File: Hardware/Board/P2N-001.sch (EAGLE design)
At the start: 37 parts, among them IC1 4053N, IC2 LTC485N, IC3 74LS07N, IC4 LTC485N, K1 G5V1, T1 2SC1815

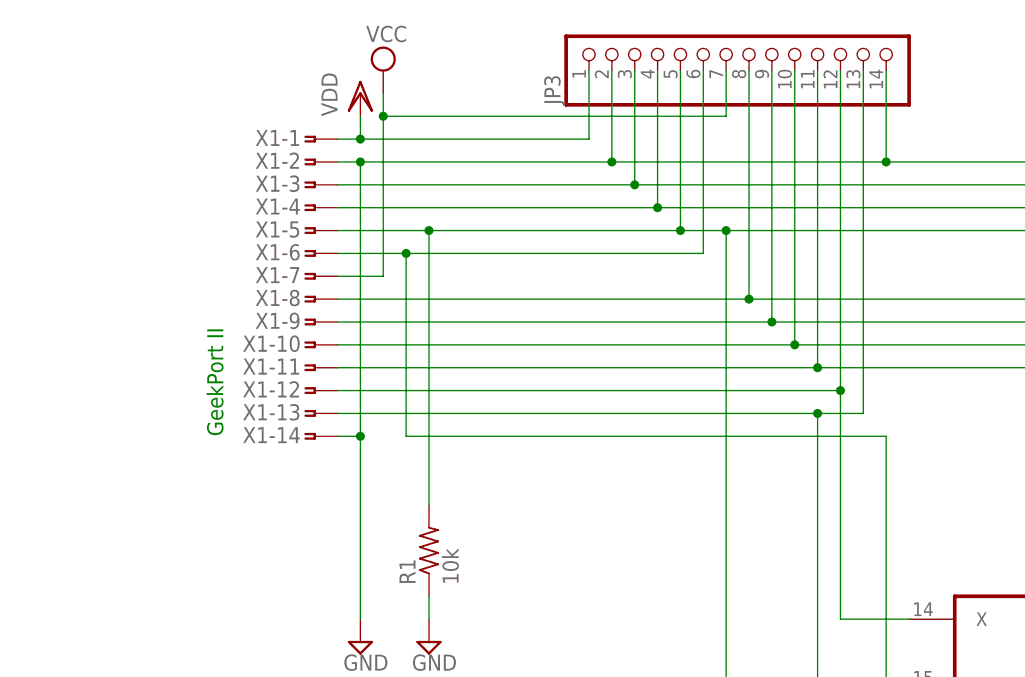
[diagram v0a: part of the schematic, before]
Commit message: Updated Hirose DX10LM1-14SE connector pattern.
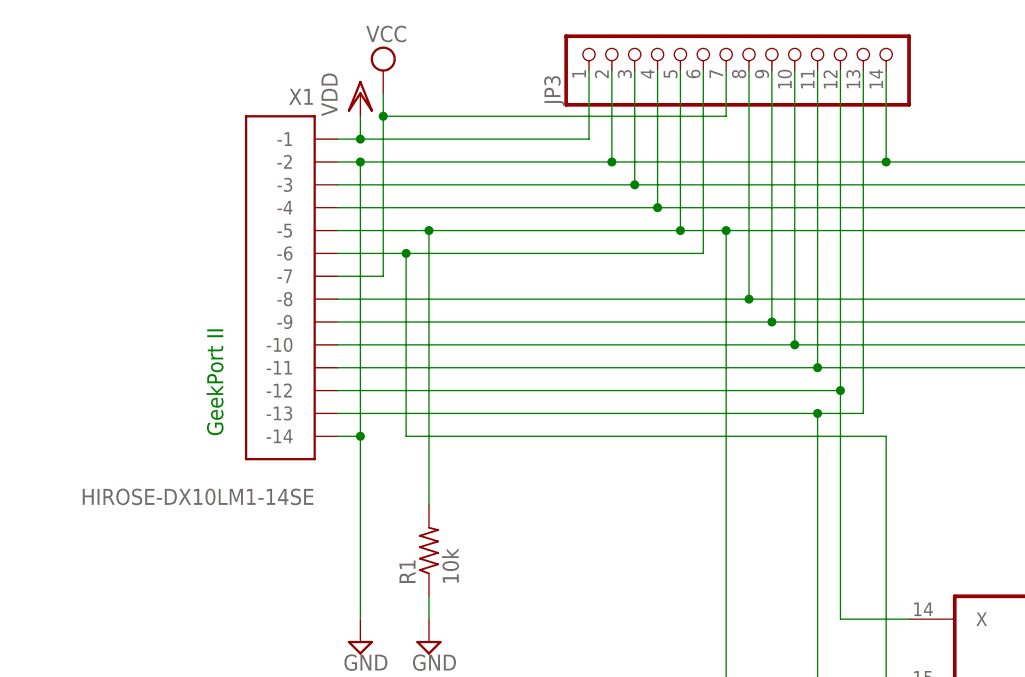
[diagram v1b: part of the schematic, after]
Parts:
- X1: value (none) -> HIROSE-DX10LM1-14SE; device con-hirose-dxlm:HIROSE-DXLM -> con-hirose-dx10lm1-14se:HIROSE-DX10LM1-14SE
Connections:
- net ANLG0: now also X1.-8; no longer X1-8.1
- net ANLG1: now also X1.-9; no longer X1-9.1
- net ANLG2: now also X1.-10; no longer X1-10.1
- net ANLG3: now also X1.-11; no longer X1-11.1
- net CD: now also X1.-6; no longer X1-6.1
- net GND: now also X1.-14, X1.-2; no longer X1-14.1, X1-2.1
- net N$28: now also X1.-12; no longer X1-12.1
- net N$29: now also X1.-13; no longer X1-13.1
- net PD: now also X1.-5; no longer X1-5.1
- net USBD+: now also X1.-3; no longer X1-3.1
- net USBD-: now also X1.-4; no longer X1-4.1
- net VCC: now also X1.-7; no longer X1-7.1
- net VDD: now also X1.-1; no longer X1-1.1
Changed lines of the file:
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@@
 <part name="SUPPLY2" library="supply2" deviceset="GND" device=""/>
 <part name="SUPPLY29" library="supply2" deviceset="GND" device=""/>
-<part name="X1" library="con-hirose-dxlm" deviceset="HIROSE-DXLM" device=""/>
 <part name="VDD1" library="supply1" deviceset="VDD" device=""/>
 <part name="SUPPLY5" library="supply2" deviceset="GND" device=""/>
@@
 <part name="SUPPLY8" library="supply2" deviceset="GND" device=""/>
 <part name="R9" library="resistor" deviceset="R-US_" device="0204/5" value="220"/>
+<part name="X1" library="con-hirose-dx10lm1-14se" deviceset="HIROSE-DX10LM1-14SE" device=""/>
 </parts>
 <sheets>
@@
 <instance part="SUPPLY2" gate="GND" x="25.4" y="129.54"/>
 <instance part="SUPPLY29" gate="GND" x="297.18" y="101.6"/>
-<instance part="X1" gate="-1" x="20.32" y="185.42" rot="MR0"/>
-<instance part="X1" gate="-2" x="20.32" y="182.88" rot="MR0"/>
-<instance part="X1" gate="-3" x="20.32" y="180.34" rot="MR0"/>
-<instance part="X1" gate="-4" x="20.32" y="177.8" rot="MR0"/>
-<instance part="X1" gate="-5" x="20.32" y="175.26" rot="MR0"/>
-<instance part="X1" gate="-6" x="20.32" y="172.72" rot="MR0"/>
-<instance part="X1" gate="-7" x="20.32" y="170.18" rot="MR0"/>
-<instance part="X1" gate="-8" x="20.32" y="167.64" rot="MR0"/>
-<instance part="X1" gate="-9" x="20.32" y="165.1" rot="MR0"/>
-<instance part="X1" gate="-10" x="20.32" y="162.56" rot="MR0"/>
-<instance part="X1" gate="-11" x="20.32" y="160.02" rot="MR0"/>
-<instance part="X1" gate="-12" x="20.32" y="157.48" rot="MR0"/>
-<instance part="X1" gate="-13" x="20.32" y="154.94" rot="MR0"/>
-<instance part="X1" gate="-14" x="20.32" y="152.4" rot="MR0"/>
 <instance part="VDD1" gate="G$1" x="7.62" y="114.3"/>
 <instance part="SUPPLY5" gate="GND" x="40.64" y="93.98"/>
@@
 <instance part="SUPPLY8" gate="GND" x="91.44" y="7.62"/>
 <instance part="R9" gate="G$1" x="228.6" y="104.14"/>
+<instance part="X1" gate="G$1" x="17.78" y="154.94" rot="MR0"/>
 </instances>
 <busses>
@@
 </segment>
 <segment>
-<pinref part="X1" gate="-2" pin="1"/>
 <pinref part="SUPPLY2" gate="GND" pin="GND"/>
 <wire x1="22.86" y1="182.88" x2="25.4" y2="182.88" width="0.1524" layer="91"/>
 <wire x1="25.4" y1="182.88" x2="25.4" y2="152.4" width="0.1524" layer="91"/>
-<pinref part="X1" gate="-14" pin="1"/>
 <wire x1="25.4" y1="152.4" x2="25.4" y2="132.08" width="0.1524" layer="91"/>
 <wire x1="22.86" y1="152.4" x2="25.4" y2="152.4" width="0.1524" layer="91"/>
@@
 <wire x1="83.82" y1="193.04" x2="83.82" y2="182.88" width="0.1524" layer="91"/>
 <junction x="83.82" y="182.88"/>
+<pinref part="X1" gate="G$1" pin="-2"/>
+<pinref part="X1" gate="G$1" pin="-14"/>
 </segment>
 <segment>
@@
 <pinref part="SUPPLY3" gate="G$1" pin="VCC"/>
 <wire x1="27.94" y1="190.5" x2="27.94" y2="187.96" width="0.1524" layer="91"/>
-<pinref part="X1" gate="-7" pin="1"/>
 <wire x1="27.94" y1="187.96" x2="27.94" y2="170.18" width="0.1524" layer="91"/>
 <wire x1="27.94" y1="170.18" x2="22.86" y2="170.18" width="0.1524" layer="91"/>
@@
 <wire x1="66.04" y1="187.96" x2="66.04" y2="193.04" width="0.1524" layer="91"/>
 <junction x="27.94" y="187.96"/>
+<pinref part="X1" gate="G$1" pin="-7"/>
 </segment>
 <segment>
@@
 </segment>
 <segment>
-<pinref part="X1" gate="-1" pin="1"/>
 <pinref part="VDD3" gate="G$1" pin="VDD"/>
 <wire x1="22.86" y1="185.42" x2="25.4" y2="185.42" width="0.1524" layer="91"/>
@@
 <wire x1="50.8" y1="185.42" x2="50.8" y2="193.04" width="0.1524" layer="91"/>
 <junction x="25.4" y="185.42"/>
+<pinref part="X1" gate="G$1" pin="-1"/>
 </segment>
 <segment>
@@
 </segment>
 <segment>
-<pinref part="X1" gate="-8" pin="1"/>
 <wire x1="127" y1="165.1" x2="124.46" y2="167.64" width="0.1524" layer="91" curve="90"/>
 <wire x1="124.46" y1="167.64" x2="68.58" y2="167.64" width="0.1524" layer="91"/>
@@
 <wire x1="68.58" y1="193.04" x2="68.58" y2="167.64" width="0.1524" layer="91"/>
 <junction x="68.58" y="167.64"/>
+<pinref part="X1" gate="G$1" pin="-8"/>
 </segment>
 </net>
@@
 </segment>
 <segment>
-<pinref part="X1" gate="-9" pin="1"/>
 <wire x1="127" y1="162.56" x2="124.46" y2="165.1" width="0.1524" layer="91" curve="90"/>
 <wire x1="124.46" y1="165.1" x2="71.12" y2="165.1" width="0.1524" layer="91"/>
@@
 <wire x1="71.12" y1="193.04" x2="71.12" y2="165.1" width="0.1524" layer="91"/>
 <junction x="71.12" y="165.1"/>
+<pinref part="X1" gate="G$1" pin="-9"/>
 </segment>
 </net>
@@
 </segment>
 <segment>
-<pinref part="X1" gate="-10" pin="1"/>
 <wire x1="127" y1="160.02" x2="124.46" y2="162.56" width="0.1524" layer="91" curve="90"/>
 <wire x1="124.46" y1="162.56" x2="73.66" y2="162.56" width="0.1524" layer="91"/>
@@
 <wire x1="73.66" y1="193.04" x2="73.66" y2="162.56" width="0.1524" layer="91"/>
 <junction x="73.66" y="162.56"/>
+<pinref part="X1" gate="G$1" pin="-10"/>
 </segment>
 </net>
@@
 </segment>
 <segment>
-<pinref part="X1" gate="-11" pin="1"/>
 <wire x1="127" y1="157.48" x2="124.46" y2="160.02" width="0.1524" layer="91" curve="90"/>
 <wire x1="124.46" y1="160.02" x2="76.2" y2="160.02" width="0.1524" layer="91"/>
@@
 <wire x1="76.2" y1="193.04" x2="76.2" y2="160.02" width="0.1524" layer="91"/>
 <junction x="76.2" y="160.02"/>
+<pinref part="X1" gate="G$1" pin="-11"/>
 </segment>
 </net>
@@
 <net name="PD" class="0">
 <segment>
-<pinref part="X1" gate="-5" pin="1"/>
 <pinref part="JP6" gate="A" pin="1"/>
 <wire x1="22.86" y1="175.26" x2="33.02" y2="175.26" width="0.1524" layer="91"/>
@@
 <label x="81.28" y="83.82" size="1.778" layer="95" rot="R90"/>
 <junction x="66.04" y="175.26"/>
+<pinref part="X1" gate="G$1" pin="-5"/>
 </segment>
 </net>
 <net name="USBD-" class="0">
 <segment>
-<pinref part="X1" gate="-4" pin="1"/>
 <pinref part="JP6" gate="A" pin="2"/>
 <wire x1="22.86" y1="177.8" x2="58.42" y2="177.8" width="0.1524" layer="91"/>
@@
 <junction x="58.42" y="177.8"/>
 <label x="111.76" y="177.8" size="1.778" layer="95"/>
+<pinref part="X1" gate="G$1" pin="-4"/>
 </segment>
 </net>
 <net name="USBD+" class="0">
 <segment>
-<pinref part="X1" gate="-3" pin="1"/>
 <pinref part="JP6" gate="A" pin="3"/>
 <wire x1="22.86" y1="180.34" x2="55.88" y2="180.34" width="0.1524" layer="91"/>
@@
 <junction x="55.88" y="180.34"/>
 <label x="111.76" y="180.34" size="1.778" layer="95"/>
+<pinref part="X1" gate="G$1" pin="-3"/>
 </segment>
 </net>
 <net name="CD" class="0">
 <segment>
-<pinref part="X1" gate="-6" pin="1"/>
 <wire x1="22.86" y1="172.72" x2="30.48" y2="172.72" width="0.1524" layer="91"/>
 <wire x1="30.48" y1="172.72" x2="30.48" y2="152.4" width="0.1524" layer="91"/>
@@
 <label x="78.74" y="55.88" size="1.778" layer="95"/>
 <label x="83.82" y="83.82" size="1.778" layer="95" rot="R90"/>
+<pinref part="X1" gate="G$1" pin="-6"/>
 </segment>
 </net>
 <net name="N$28" class="0">
 <segment>
-<pinref part="X1" gate="-12" pin="1"/>
 <wire x1="22.86" y1="157.48" x2="78.74" y2="157.48" width="0.1524" layer="91"/>
 <wire x1="78.74" y1="157.48" x2="78.74" y2="132.08" width="0.1524" layer="91"/>
@@
 <wire x1="78.74" y1="193.04" x2="78.74" y2="157.48" width="0.1524" layer="91"/>
 <junction x="78.74" y="157.48"/>
+<pinref part="X1" gate="G$1" pin="-12"/>
 </segment>
 </net>
 <net name="N$29" class="0">
 <segment>
-<pinref part="X1" gate="-13" pin="1"/>
 <wire x1="22.86" y1="154.94" x2="76.2" y2="154.94" width="0.1524" layer="91"/>
 <wire x1="76.2" y1="154.94" x2="76.2" y2="124.46" width="0.1524" layer="91"/>
@@
 <wire x1="76.2" y1="124.46" x2="86.36" y2="124.46" width="0.1524" layer="91"/>
 <wire x1="76.2" y1="154.94" x2="81.28" y2="154.94" width="0.1524" layer="91"/>
-<wire x1="81.28" y1="154.94" x2="81.28" y2="175.26" width="0.1524" layer="91"/>
+<wire x1="81.28" y1="154.94" x2="81.28" y2="193.04" width="0.1524" layer="91"/>
 <pinref part="JP3" gate="A" pin="13"/>
 <junction x="76.2" y="154.94"/>
-<wire x1="81.28" y1="175.26" x2="81.28" y2="193.04" width="0.1524" layer="91"/>
-</segment>
-</net>
+<pinref part="X1" gate="G$1" pin="-13"/>
+</segment>
+</net>

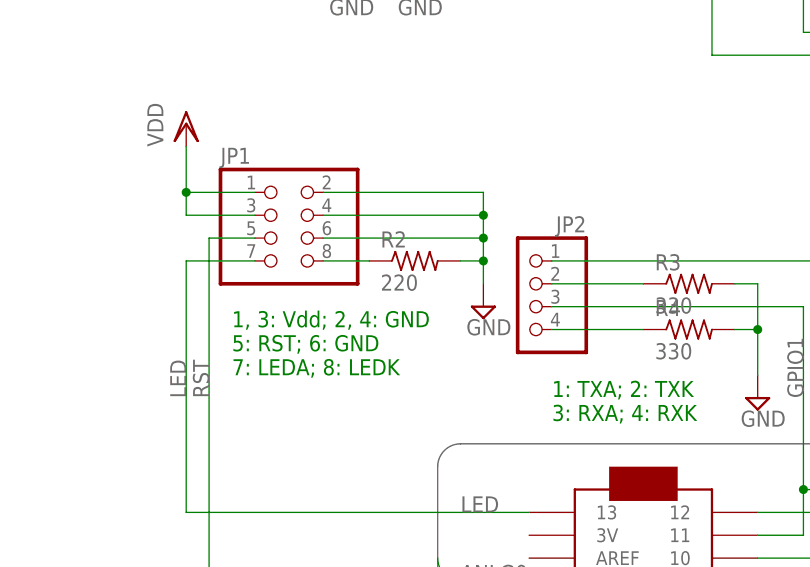
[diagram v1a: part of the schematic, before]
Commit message: Changed R value of main LED (from 220 to 150 ohm).
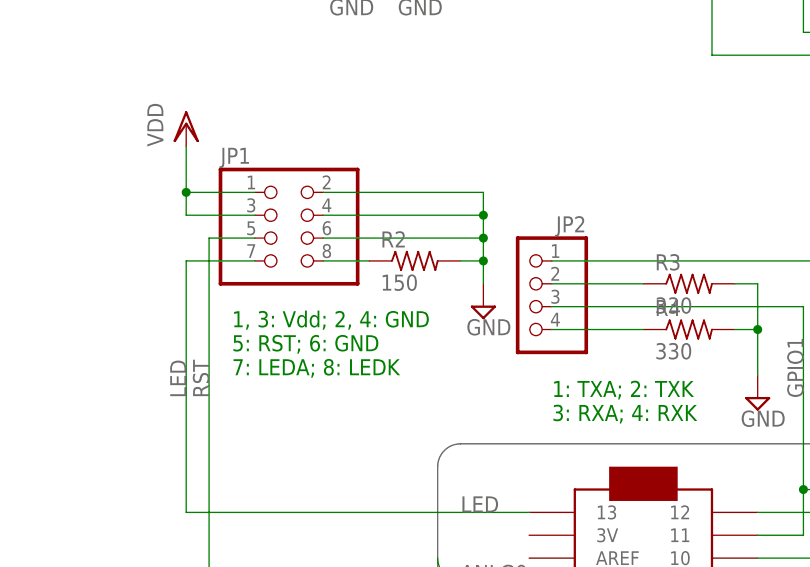
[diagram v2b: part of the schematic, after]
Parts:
- R2: value 220 -> 150
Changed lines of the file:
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@@
 <part name="SUPPLY9" library="supply2" deviceset="GND" device=""/>
 <part name="VDD3" library="supply1" deviceset="VDD" device=""/>
-<part name="R2" library="resistor" deviceset="R-US_" device="0204/5" value="220"/>
+<part name="R2" library="resistor" deviceset="R-US_" device="0204/5" value="150"/>
 <part name="SV1" library="con-ml" deviceset="ML10L" device=""/>
 <part name="JP6" library="pinhead" deviceset="PINHD-1X5" device="/90"/>

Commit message: Changed 10p-backport to 14p-backport.
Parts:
- removed JP5: (no value), pinhead:PINHD-2X3
- removed JP6: (no value), pinhead:PINHD-1X5/90
- added LED1, LED2: (no value), led:LED3MM
- added R12: 120, resistor:R-US_0204/5
- JP2: device pinhead:PINHD-1X4 -> pinhead:PINHD-1X14
- JP3: device pinhead:PINHD-1X14 -> pinhead:PINHD-2X3
- JP4: device pinhead:PINHD-1X2/90 -> pinhead:PINHD-1X5/90
- R1: value 10k -> 150
- R11, R6: value 120 -> 220
- R2: value 150 -> 10k
- R7: value 220 -> 120
- SV1: device con-ml:ML10L -> con-ml:ML14L
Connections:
- removed net SX: JP4.1, MC1.10
- removed net SY: JP4.2, MC1.9
- new net N$5: R10.2, SV1.11
- new net SENS0: MC1.10, SV1.13
- new net SENS1: MC1.9, SV1.14
- net ANLG0: now also JP2.8; no longer JP3.8
- net ANLG1: now also JP2.9; no longer JP3.9
- net ANLG2: now also JP2.10; no longer JP3.10
- net ANLG3: now also JP2.11; no longer JP3.11
- net CA: now also SV1.1; no longer SV1.6
- net CB: now also SV1.3; no longer SV1.8
- net CD: now also JP2.6; no longer JP3.6
- net GND: now also JP2.14, JP2.2, JP4.5, R1.2, R2.1, SV1.7; no longer JP3.14, JP3.2, JP6.5, R1.1, R2.2
- net GPIO0: now also JP3.1, LED1.A; no longer JP2.1, JP5.1
- net GPIO1: now also JP3.2, LED2.A; no longer JP2.3, JP5.2
- net GPIO2: now also JP3.3; no longer JP5.3
- net MISO: now also JP3.4; no longer JP5.4
- net MOSI: now also JP3.5; no longer JP5.5
- net N$15: now also R8.1; no longer R7.1
- net N$17: now also LED1.C; no longer JP2.2
- net N$18: now also LED2.C; no longer JP2.4
- net N$2: now also R11.1; no longer R10.1
- net N$28: now also JP2.12; no longer JP3.12
- net N$29: now also JP2.13; no longer JP3.13
- net N$3: now also R6.1; no longer R9.1
- net N$32: now also R1.1; no longer R2.1
- net N$4: now also R6.2, SV1.12; no longer R9.2, SV1.7
- net PD: now also JP2.5, JP4.1, R2.2; no longer JP3.5, JP6.1, R1.2
- net RAWTX: now also SV1.8; no longer SV1.3
- net RETURN: now also R11.2; no longer R10.2
- net RX+: now also R7.2; no longer R6.2
- net RX-: now also R7.1; no longer R6.1
- net RXA: now also R8.2; no longer R7.2
- net SCLK: now also JP3.6; no longer JP5.6
- net SEND: now also R9.2; no longer R8.2
- net TX+: now also R12.2; no longer R11.2
- net TX-: now also R12.1; no longer R11.1
- net USBD+: now also JP2.3, JP4.3; no longer JP3.3, JP6.3
- net USBD-: now also JP2.4, JP4.2; no longer JP3.4, JP6.2
- net VCC: now also JP2.7, R10.1, R9.1, SV1.6; no longer JP3.7, R8.1, SV1.1
- net VDD: now also JP2.1; no longer JP3.1
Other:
- note added: "1: Contact A; 2: GND; 3: Contact B; 4: MIDI OUT Send; 5: MIDI OUT Return; 6: Vcc; 7: GND; 8: Raw TX; 9: MIDI IN Anode; 10: MIDI IN Kathode; 11: MIDI THRU Send; 12: MIDI THRU Return; 13: Sensor X; 14: Sensor Y"
- note added: "1: GPIO 0; 2: GPIO 1; 2: GPIO 3; 4: MISO; 5: MOSI; 6: SCLCK"
- note removed: "1: Sensor X 2: Sensor Y"
- note removed: "1: Sensor X; 2: Sensor Y 3: GPIO; 4: MISO 5: MOSI; 6: SCLCK"
- note removed: "1: Vcc; 2: GND 3: Raw TX; 4: MIDI OUT Send; 5: MIDI OUT Return 6: Contact A; 7: GND; 8: Contact B 9: MIDI IN Anode; 10: MIDI IN Kathode"
- moved on the sheet: CN1, IC1, IC3C, IC3D, IC3E, IC3F, JP1, R1, R10, R11, R2, R6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

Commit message: Adopted to XMIDI.
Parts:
- added R13: 220, resistor:R-US_0204/5
- added R14: 120, resistor:R-US_0204/5
- R12: value 120 -> 220
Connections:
- removed net CA: K12.P, SV1.1
- removed net CB: K12.S, SV1.3
- removed net N$5: R10.2, SV1.11
- removed net RAWTX: IC3B.O, SV1.8
- removed net RETURN: R11.2, SV1.5
- removed net SEND: R9.2, SV1.4
- new net RXRETURN: R6.2, SV1.3
- new net RXSEND: R11.2, SV1.1
- new net TXRETURN: R13.2, SV1.8
- new net TXRETURNII: R12.2, SV1.5
- new net TXSEND: R9.2, SV1.6
- new net TXSENDZV: R10.2, SV1.14, SV1.4
- new net ZVA: K12.P, SV1.11
- new net ZVB: K12.S, SV1.13
- net GND: now also SV1.12
- net N$2: now also R12.1; no longer R11.1
- net N$4: now also IC3B.O, R13.1; no longer R6.2, SV1.12
- net SENS0: no longer SV1.13
- net SENS1: no longer SV1.14
- net TX+: now also R14.2; no longer R12.2
- net TX-: now also R14.1; no longer R12.1
- net VCC: now also R11.1; no longer SV1.6
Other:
- note added: "1: RX Send; 2: GND; 3: RX Return; 4: TX Send ZV; 5: TX Return II; 6: TX Send; 7: GND; 8: TX Return; 9: RX Anode; 10: RX Kathode; 11: ZV Contact A; 12: GND; 13: ZV Contact B; 14: Vcc R220"
- note removed: "1: Contact A; 2: GND; 3: Contact B; 4: MIDI OUT Send; 5: MIDI OUT Return; 6: Vcc; 7: GND; 8: Raw TX; 9: MIDI IN Anode; 10: MIDI IN Kathode; 11: MIDI THRU Send; 12: MIDI THRU Return; 13: Sensor X; 14: Sensor Y"
- moved on the sheet: R10, R11, R12, R9

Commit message: Cleaned up board design.
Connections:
- net TXRETURNII renamed TX2RETURN
- net TXSENDZV renamed TX2SEND
- removed net SENS0: MC1.10
- removed net SENS1: MC1.9
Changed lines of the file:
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@@
-</segment>
-</bus>
-<bus name="SENS[0..1]">
-<segment>
-<wire x1="104.14" y1="63.5" x2="104.14" y2="68.58" width="0.762" layer="92"/>
-<wire x1="104.14" y1="68.58" x2="106.68" y2="71.12" width="0.762" layer="92" curve="-90"/>
-<wire x1="106.68" y1="71.12" x2="124.46" y2="71.12" width="0.762" layer="92"/>
-<wire x1="124.46" y1="71.12" x2="127" y2="73.66" width="0.762" layer="92" curve="90"/>
-<wire x1="127" y1="73.66" x2="127" y2="142.24" width="0.762" layer="92"/>
-<wire x1="127" y1="142.24" x2="129.54" y2="144.78" width="0.762" layer="92" curve="-90"/>
-<wire x1="129.54" y1="144.78" x2="307.34" y2="144.78" width="0.762" layer="92"/>
 </segment>
 </bus>
@@
 </segment>
 </net>
-<net name="TXRETURNII" class="0">
+<net name="TX2RETURN" class="0">
 <segment>
 <pinref part="R12" gate="G$1" pin="2"/>
@@
 </segment>
 </net>
-<net name="TXSENDZV" class="0">
+<net name="TX2SEND" class="0">
 <segment>
 <pinref part="R10" gate="G$1" pin="2"/>
@@
 </segment>
 </net>
-<net name="SENS0" class="0">
-<segment>
-<pinref part="MC1" gate="G$1" pin="10"/>
-<wire x1="104.14" y1="68.58" x2="101.6" y2="66.04" width="0.1524" layer="91" curve="-90"/>
-<wire x1="101.6" y1="66.04" x2="71.12" y2="66.04" width="0.1524" layer="91"/>
-<label x="86.36" y="66.04" size="1.778" layer="95"/>
-</segment>
-</net>
-<net name="SENS1" class="0">
-<segment>
-<pinref part="MC1" gate="G$1" pin="9"/>
-<wire x1="104.14" y1="66.04" x2="101.6" y2="63.5" width="0.1524" layer="91" curve="-90"/>
-<wire x1="101.6" y1="63.5" x2="71.12" y2="63.5" width="0.1524" layer="91"/>
-<label x="86.36" y="63.5" size="1.778" layer="95"/>
-</segment>
-</net>
